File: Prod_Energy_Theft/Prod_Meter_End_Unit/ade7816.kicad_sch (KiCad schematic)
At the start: 56 parts, among them J1 Screw_Terminal_01x02, J10 Screw_Terminal_01x02, J11 Screw_Terminal_01x02, J15 Screw_Terminal_01x01, J16 Screw_Terminal_01x01, J2 Screw_Terminal_01x02, J3 Screw_Terminal_01x02, J4 Screw_Terminal_01x02, U5 ADE7816ACPZ, Y2 Crystal

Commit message: Chnages in power and ADE7816
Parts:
- removed C24, C25: 22nf, Capacitor_SMD:C_0805_2012Metric, symbol Device:C
- removed J15, J16: Screw_Terminal_01x01, custom:TerminalBlock_1x01_P5.08mm, symbol Connector:Screw_Terminal_01x01
- removed R18, R19: 10k, Resistor_SMD:R_0805_2012Metric, symbol Device:R
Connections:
- net GND: now also J1.2 (Pin_2), J10.2 (Pin_2), J11.2 (Pin_2), J2.2 (Pin_2), J3.2 (Pin_2), J4.2 (Pin_2), R10.1, R20.2, R21.2, R22.2, R23.1, R25.1, R41.2, R42.1, R44.2, R45.1, R47.2, R48.1
- no-connect marks 4 -> 6
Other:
- moved on the sheet: C40

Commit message: PCB
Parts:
- J1, J10, J11, J2, J3, J4: footprint TerminalBlock_Phoenix:TerminalBlock_Phoenix_PTSM-0,5-2-2,5-V-SMD_1x02-1MP_P2.50mm_Vertical -> TerminalBlock_Phoenix:TerminalBlock_Phoenix_MKDS-1,5-2-5.08_1x02_P5.08mm_Horizontal
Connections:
- net +3.3V is gone; now on net +3.3V_ADE: R27.1, R28.2, U5.2 (PULL_HIGH)
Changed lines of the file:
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@@
 			)
 		)
-		(property "Footprint" "TerminalBlock_Phoenix:TerminalBlock_Phoenix_PTSM-0,5-2-2,5-V-SMD_1x02-1MP_P2.50mm_Vertical"
+		(property "Footprint" "TerminalBlock_Phoenix:TerminalBlock_Phoenix_MKDS-1,5-2-5.08_1x02_P5.08mm_Horizontal"
 			(at 24.13 105.41 0)
 			(effects
@@
 			)
 		)
-		(property "Footprint" "TerminalBlock_Phoenix:TerminalBlock_Phoenix_PTSM-0,5-2-2,5-V-SMD_1x02-1MP_P2.50mm_Vertical"
+		(property "Footprint" "TerminalBlock_Phoenix:TerminalBlock_Phoenix_MKDS-1,5-2-5.08_1x02_P5.08mm_Horizontal"
 			(at 24.13 168.91 0)
 			(effects
@@
 			)
 		)
-		(property "Footprint" "TerminalBlock_Phoenix:TerminalBlock_Phoenix_PTSM-0,5-2-2,5-V-SMD_1x02-1MP_P2.50mm_Vertical"
+		(property "Footprint" "TerminalBlock_Phoenix:TerminalBlock_Phoenix_MKDS-1,5-2-5.08_1x02_P5.08mm_Horizontal"
 			(at 96.52 168.91 0)
 			(effects
@@
 			)
 		)
-		(property "Value" "+3.3V"
+		(property "Value" "+3.3V_ADE"
 			(at 163.322 119.634 0)
 			(effects
@@
 			)
 		)
-		(property "Footprint" "TerminalBlock_Phoenix:TerminalBlock_Phoenix_PTSM-0,5-2-2,5-V-SMD_1x02-1MP_P2.50mm_Vertical"
+		(property "Footprint" "TerminalBlock_Phoenix:TerminalBlock_Phoenix_MKDS-1,5-2-5.08_1x02_P5.08mm_Horizontal"
 			(at 24.13 29.21 0)
 			(effects
@@
 			)
 		)
-		(property "Value" "+3.3V"
+		(property "Value" "+3.3V_ADE"
 			(at 251.46 113.0299 90)
 			(effects
@@
 			)
 		)
-		(property "Footprint" "TerminalBlock_Phoenix:TerminalBlock_Phoenix_PTSM-0,5-2-2,5-V-SMD_1x02-1MP_P2.50mm_Vertical"
+		(property "Footprint" "TerminalBlock_Phoenix:TerminalBlock_Phoenix_MKDS-1,5-2-5.08_1x02_P5.08mm_Horizontal"
 			(at 24.13 71.12 0)
 			(effects
@@
 		(on_board yes)
 		(dnp no)
-		(fields_autoplaced yes)
 		(property "Reference" "#PWR058"
 			(at 163.83 80.01 0)
@@
 			)
 		)
-		(property "Value" "+3.3V"
-			(at 163.83 71.12 0)
+		(property "Value" "+3.3V_ADE"
+			(at 160.782 70.866 0)
 			(effects
 				(font
@@
 			)
 		)
-		(property "Footprint" "TerminalBlock_Phoenix:TerminalBlock_Phoenix_PTSM-0,5-2-2,5-V-SMD_1x02-1MP_P2.50mm_Vertical"
+		(property "Footprint" "TerminalBlock_Phoenix:TerminalBlock_Phoenix_MKDS-1,5-2-5.08_1x02_P5.08mm_Horizontal"
 			(at 24.13 135.89 0)
 			(effects

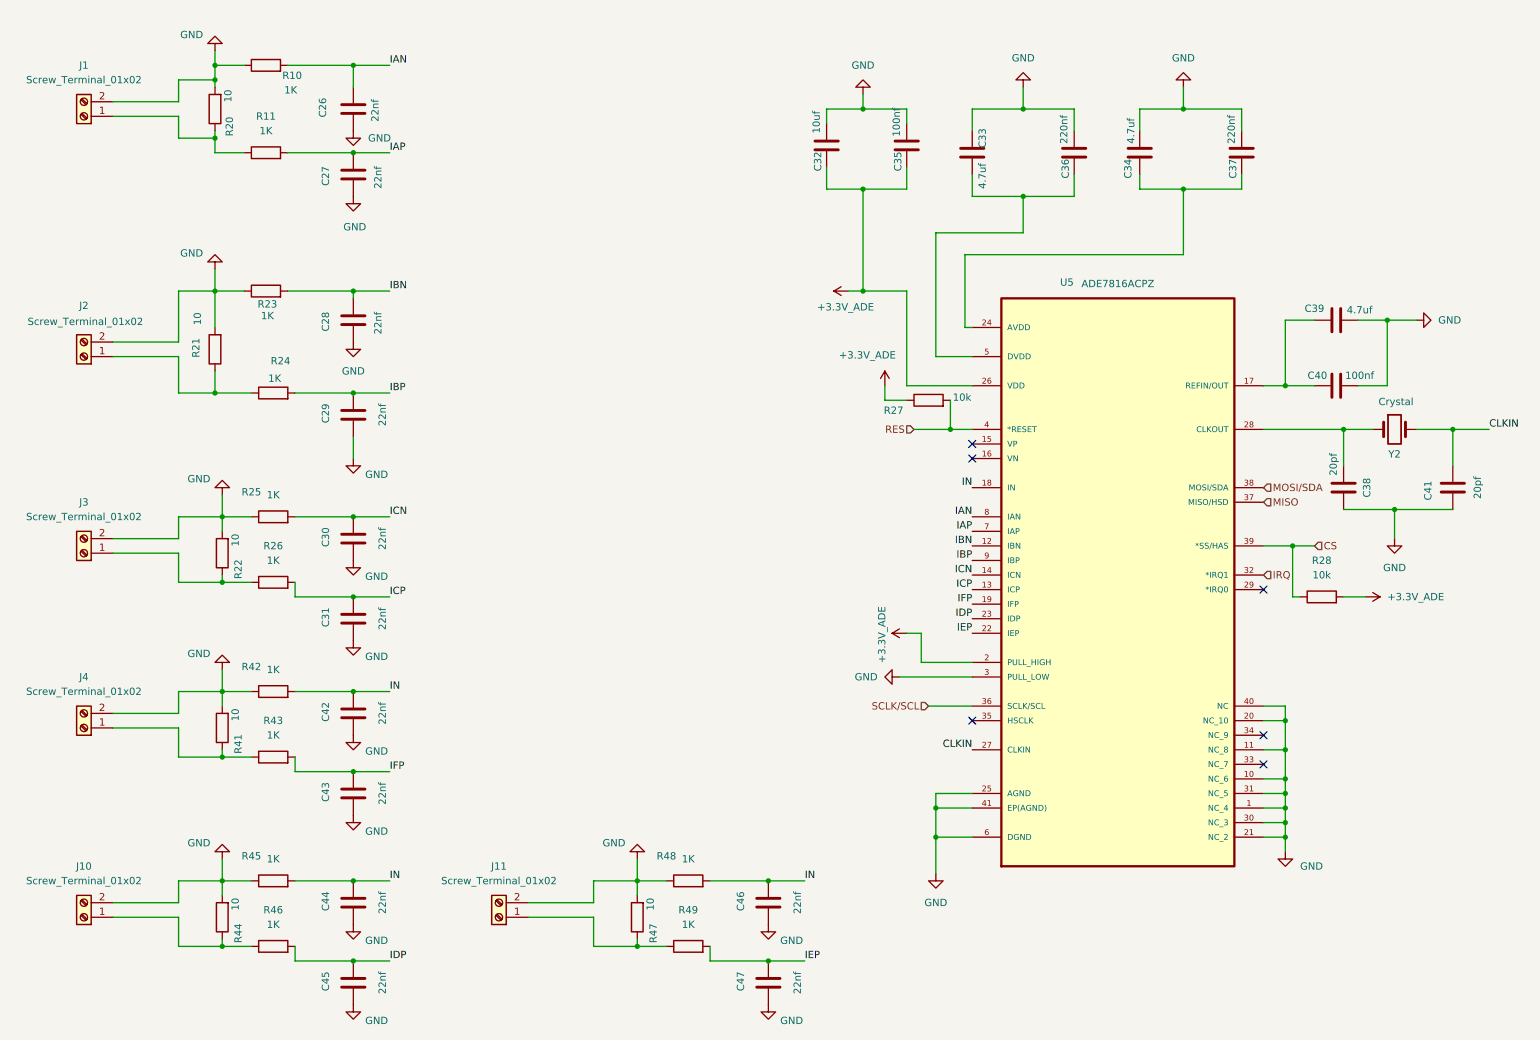
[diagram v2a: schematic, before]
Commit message: update in BOM list
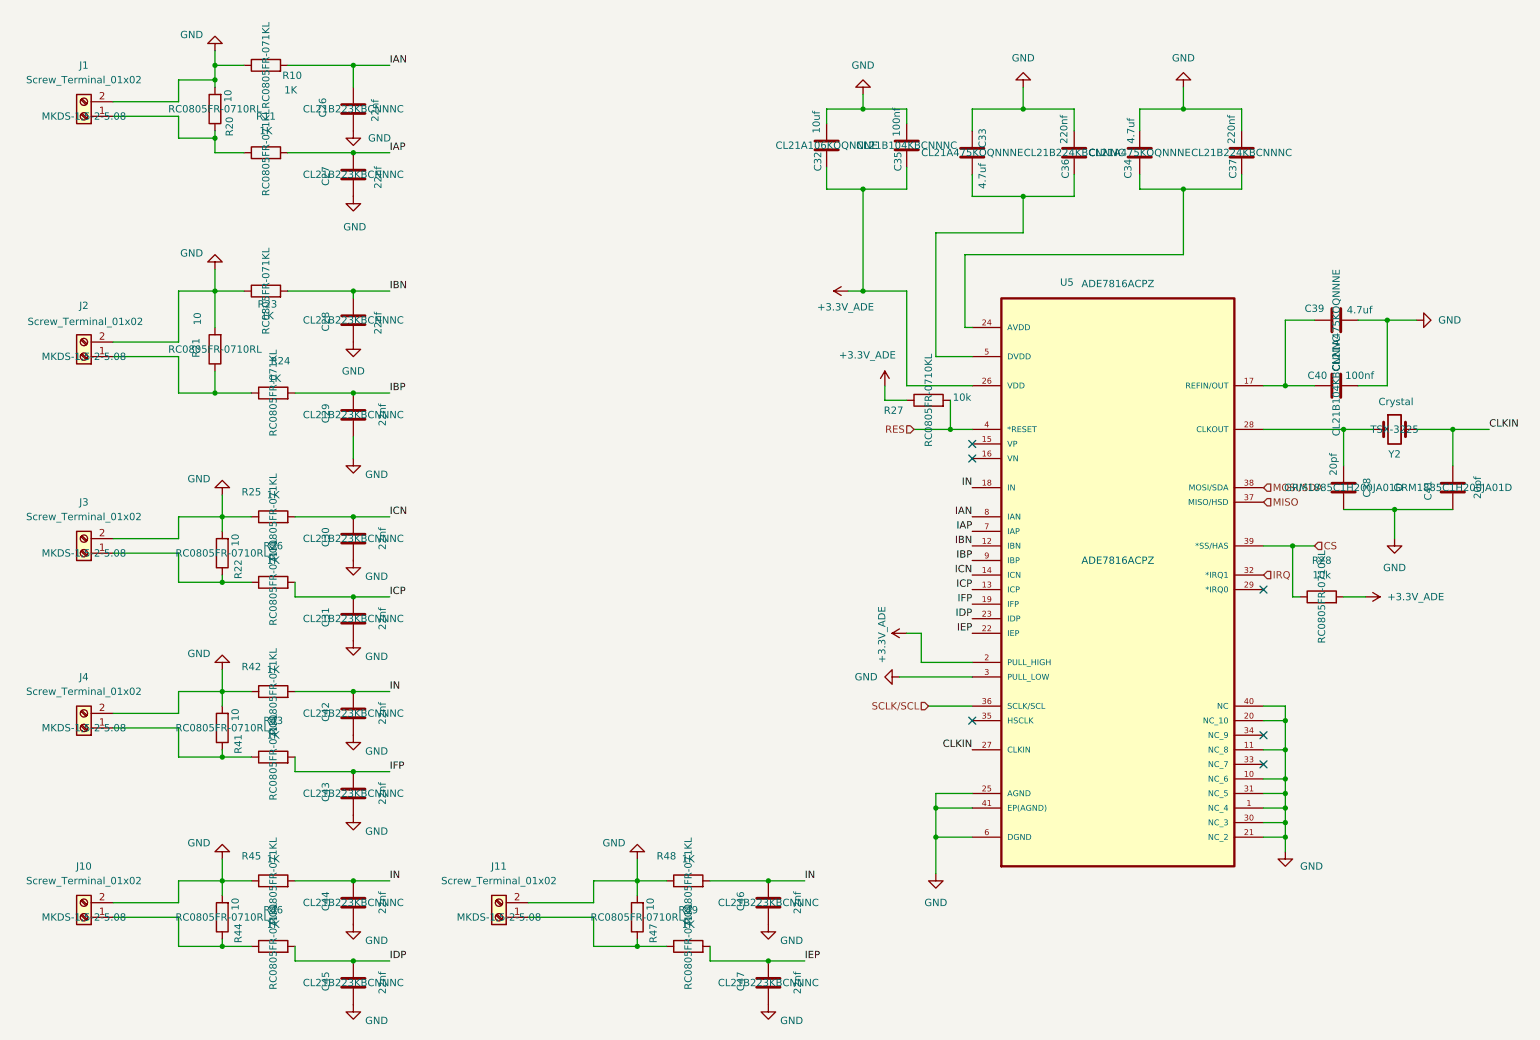
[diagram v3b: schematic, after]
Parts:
- C26, C27, C28, C29, C30, C31, C42, C43, C44, C45, C46, C47: Part Number (none) -> CL21B223KBCNNNC
- C32: Part Number (none) -> CL21A106KOQNNNE
- C33, C34, C39: Part Number (none) -> CL21A475KOQNNNE
- C35, C40: Part Number (none) -> CL21B104KBCNNNC
- C36, C37: Part Number (none) -> CL21B224KBCNNNC
- C38, C41: Part Number (none) -> GRM1885C1H200JA01D
- J1, J10, J11, J2, J3, J4: Part Number (none) -> MKDS-1,5-2-5.08
- R10, R11, R23, R24, R25, R26, R42, R43, R45, R46, R48, R49: Part Number (none) -> RC0805FR-071KL
- R20, R21, R22, R41, R44, R47: Part Number (none) -> RC0805FR-0710RL
- R27, R28: Part Number (none) -> RC0805FR-0710KL
- U5: Part Number (none) -> ADE7816ACPZ
- Y2: Part Number (none) -> TSX-3225
